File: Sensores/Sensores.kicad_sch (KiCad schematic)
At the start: 18 parts, among them IC1 LF353, J1 GFCI, J2 NTC 3950, J3 PZEM 00T 100A, J4 ALIMENTACION

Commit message: footprint del pzem 004t
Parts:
- J3: value PZEM 00T 100A -> PZEM 004T 100A; footprint Connector_JST:JST_EH_B4B-EH-A_1x04_P2.50mm_Vertical -> PZEM:PZEM
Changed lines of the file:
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@@
   (symbol (lib_id "Connector_Generic:Conn_01x04") (at 67.437 37.846 180) (unit 1)
     (in_bom yes) (on_board yes) (dnp no) (fields_autoplaced)
-    (property "Reference" "J3" (at 67.437 27.686 0)
+    (property "Reference" "J3" (at 67.437 27.94 0)
       (effects (font (size 1.27 1.27)))
     )
-    (property "Value" "PZEM 00T 100A" (at 67.437 30.226 0)
+    (property "Value" "PZEM 004T 100A" (at 67.437 30.48 0)
       (effects (font (size 1.27 1.27)))
     )
-    (property "Footprint" "Connector_JST:JST_EH_B4B-EH-A_1x04_P2.50mm_Vertical" (at 67.437 37.846 0)
+    (property "Footprint" "PZEM:PZEM" (at 67.437 37.846 0)
       (effects (font (size 1.27 1.27)) hide)
     )

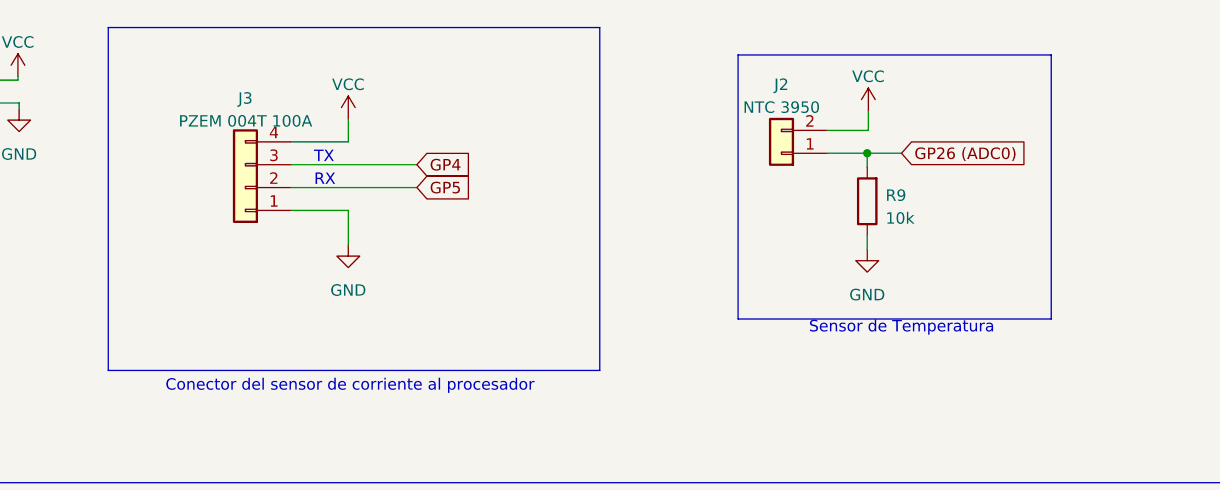
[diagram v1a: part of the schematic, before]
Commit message: correción de algunas referencias
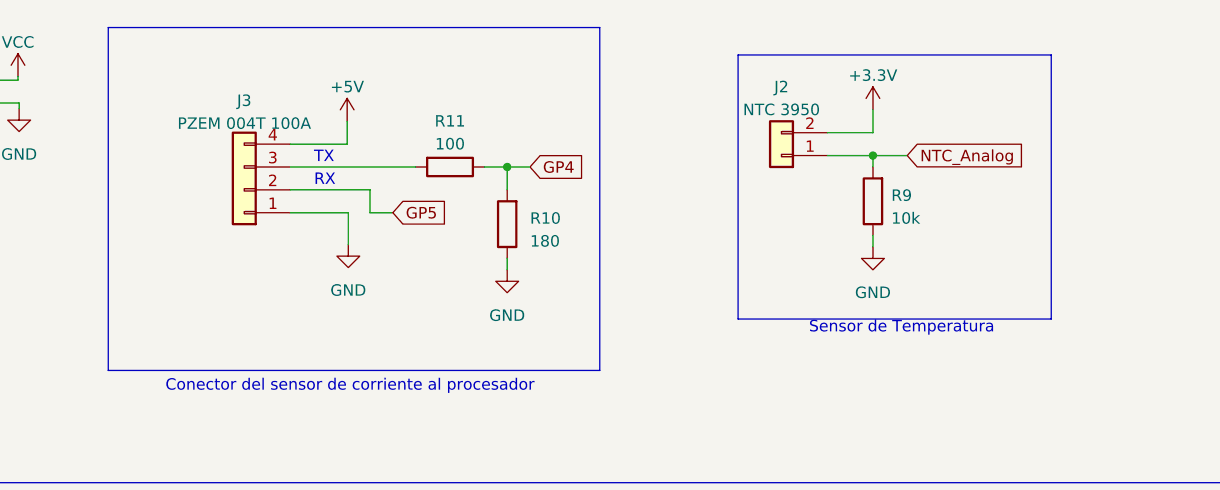
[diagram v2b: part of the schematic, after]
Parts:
- added R10: 180, Resistor_SMD:R_1206_3216Metric_Pad1.30x1.75mm_HandSolder, symbol Device:R
- added R11: 100, Resistor_SMD:R_1206_3216Metric_Pad1.30x1.75mm_HandSolder, symbol Device:R
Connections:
- net GND: now also R10.1
- net GP4: now also R10.2, R11.1; no longer J3.3 (Pin_3)
- net VCC: no longer J2.2 (Pin_2), J3.4 (Pin_4)
- net GP26 (ADC0) renamed NTC_Analog
- new net: J3.3 (Pin_3), R11.2
- new net +3.3V: J2.2 (Pin_2)
- new net +5V: J3.4 (Pin_4)
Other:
- moved on the sheet: R9
